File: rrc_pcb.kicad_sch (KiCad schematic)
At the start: 15 parts, among them J1 Conn_01x02_Male-Connector, J2 Conn_01x03_Male-Connector, J3 digital logic connection, U1 iridium9602, U2 Teensy4.1, U3 BN220-GPS, U4 ICM-20948, U5 MS5611, U6 logo, U7 voltReg

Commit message: Edit of PCB
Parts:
- removed U1: iridium9602, iridium9602:iridium9602, symbol parts:iridium9602
- added RF1: RFD900+-RF_Module, rfd900+:RFD900+, symbol parts:RFD900+-RF_Module
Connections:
- net GND: now also RF1.2 (GND)
- net RX2: now also RF1.9 (SITX)
- net TX2: now also RF1.7 (SIRX)
- net VCC: now also U4.24 (AD0/SDO), RF1.4 (+5V)

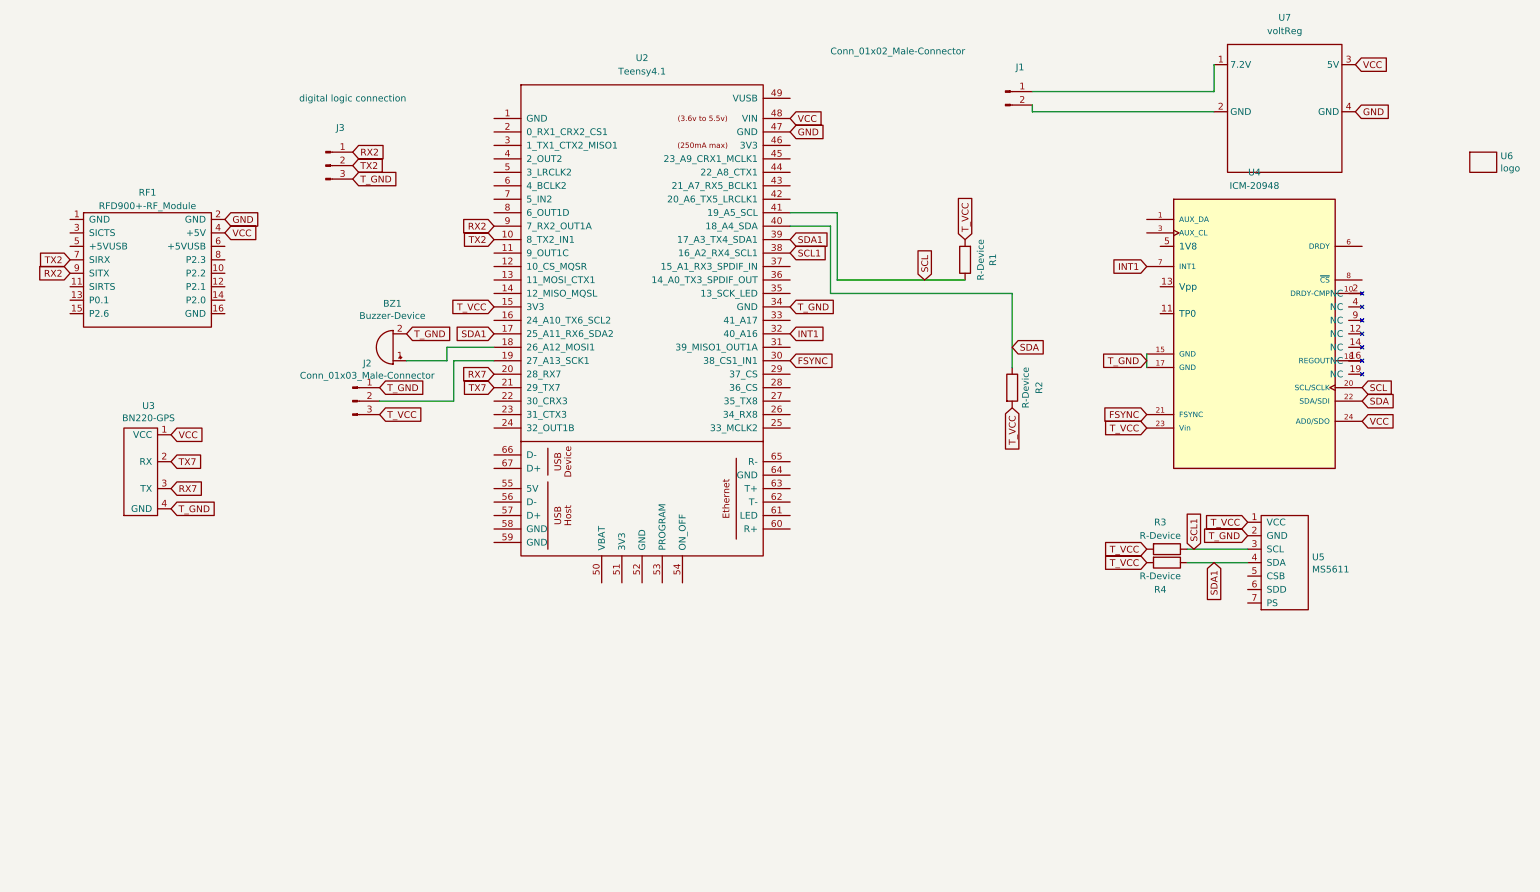
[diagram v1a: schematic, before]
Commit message: updated pcb ina160 and traces
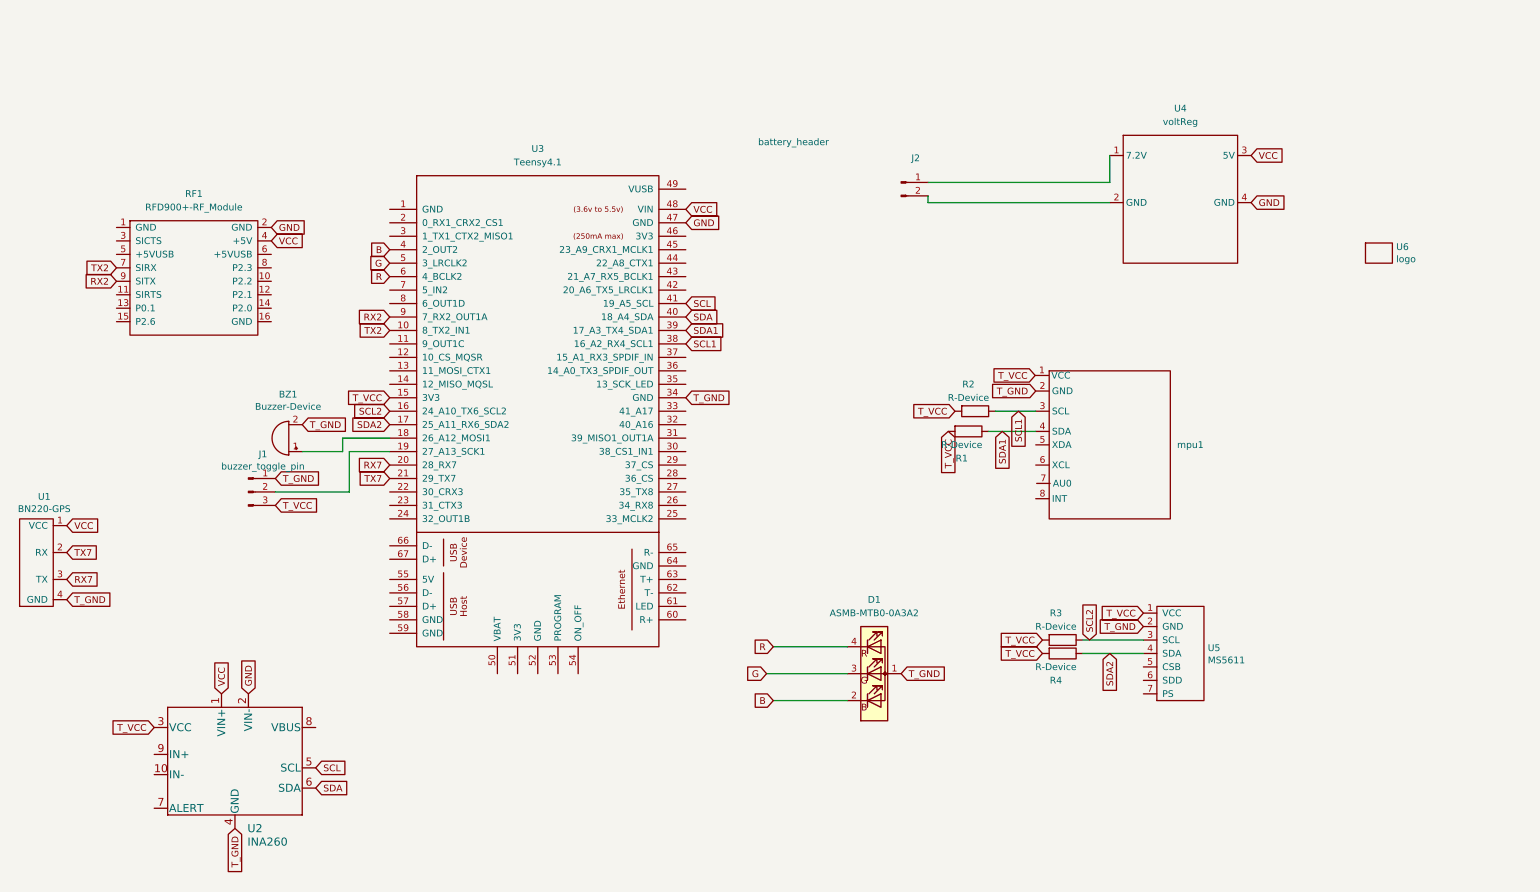
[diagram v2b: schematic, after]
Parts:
- removed J1: Conn_01x02_Male-Connector, Connector_AMASS:AMASS_XT30U-F_1x02_P5.0mm_Vertical, symbol rrc_pcb-rescue:Conn_01x02_Male-Connector
- removed J2: Conn_01x03_Male-Connector, Connector_PinHeader_2.54mm:PinHeader_1x03_P2.54mm_Vertical, symbol rrc_pcb-rescue:Conn_01x03_Male-Connector
- removed J3: digital logic connection, Connector_PinHeader_2.54mm:PinHeader_1x03_P2.54mm_Vertical, symbol rrc_pcb-rescue:Conn_01x03_Male-Connector
- removed U2: Teensy4.1, teensy:Teensy41, symbol teensy:Teensy4.1
- removed U3: BN220-GPS, bn220_gps:BN220, symbol parts:BN220-GPS
- removed U4: ICM-20948, icm20948:icm20948, symbol parts:ICM-20948
- removed U7: voltReg, VoltReg:voltReg, symbol parts:voltReg
- added D1: ASMB-MTB0-0A3A2, LED_4pin:LED_4PIN, symbol LED:ASMB-MTB0-0A3A2
- added J1: buzzer_toggle_pin, Connector_PinHeader_2.54mm:PinHeader_1x03_P2.54mm_Vertical, symbol rrc_pcb-rescue:Conn_01x03_Male-Connector
- added J2: battery_header, Connector_JST:JST_GH_SM02B-GHS-TB_1x02-1MP_P1.25mm_Horizontal, symbol rrc_pcb-rescue:Conn_01x02_Male-Connector
- added U1: BN220-GPS, bn220_gps:BN220, symbol parts:BN220-GPS
- added U2: INA260, INA260:INA260, symbol parts:INA260
- added U3: Teensy4.1, teensy:Teensy41, symbol teensy:Teensy4.1
- added U4: voltReg, VoltReg:voltReg, symbol parts:voltReg
- added mpu1: ~, MPU6050:MPU6050, symbol parts:mpu6050_eval
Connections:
- net GND: now also U2.2 (VIN-), U3.47 (GND), U4.4 (GND)
- net RX2: now also U3.9 (7_RX2_OUT1A)
- net RX7: now also U1.3 (TX), U3.20 (28_RX7)
- net SCL: now also U2.5 (SCL), U3.41 (19_A5_SCL); no longer R1.1
- net SCL1: now also R2.1, U3.38 (16_A2_RX4_SCL1), mpu1.3 (SCL); no longer R3.1, U5.3 (SCL)
- net SDA: now also U2.6 (SDA), U3.40 (18_A4_SDA); no longer R2.1
- net SDA1: now also R1.1, U3.39 (17_A3_TX4_SDA1), mpu1.4 (SDA); no longer R4.1, U5.4 (SDA)
- net TX2: now also U3.10 (8_TX2_IN1)
- net TX7: now also U1.2 (RX), U3.21 (29_TX7)
- net T_GND: now also D1.1 (A), J1.1 (Pin_1), U1.4 (GND), U2.4 (GND), U3.34 (GND), mpu1.2 (GND)
- net T_VCC: now also J1.3 (Pin_3), U2.3 (VCC), U3.15 (3V3), mpu1.1 (VCC)
- net VCC: now also U1.1 (VCC), U2.1 (VIN+), U3.48 (VIN), U4.3 (5V)
- net at BZ1.1 (-): now also U3.18 (26_A12_MOSI1)
- new net: J2.1 (Pin_1), U4.1 (7.2V)
- new net: J2.2 (Pin_2), U4.2 (GND)
- new net: J1.2 (Pin_2), U3.19 (27_A13_SCK1)
- new net B: D1.2 (BK), U3.4 (2_OUT2)
- new net G: D1.3 (GK), U3.5 (3_LRCLK2)
- new net R: D1.4 (RK), U3.6 (4_BCLK2)
- new net SCL2: R3.1, U3.16 (24_A10_TX6_SCL2), U5.3 (SCL)
- new net SDA2: R4.1, U3.17 (25_A11_RX6_SDA2), U5.4 (SDA)
